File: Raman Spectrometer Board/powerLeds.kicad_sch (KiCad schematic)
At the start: 6 parts

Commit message: tof voltages connected
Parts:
- D1, D2, D3: footprint LED_SMD:LED_0201_0603Metric_Pad0.64x0.40mm_HandSolder -> (none)
- R1, R2, R3: footprint Resistor_SMD:R_0201_0603Metric_Pad0.64x0.40mm_HandSolder -> (none)
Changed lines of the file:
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@@
 			)
 		)
-		(property "Footprint" "LED_SMD:LED_0201_0603Metric_Pad0.64x0.40mm_HandSolder"
+		(property "Footprint" ""
 			(at 123.19 93.98 0)
 			(effects
@@
 			)
 		)
-		(property "Footprint" "LED_SMD:LED_0201_0603Metric_Pad0.64x0.40mm_HandSolder"
+		(property "Footprint" ""
 			(at 138.43 93.98 0)
 			(effects
@@
 			)
 		)
-		(property "Footprint" "Resistor_SMD:R_0201_0603Metric_Pad0.64x0.40mm_HandSolder"
+		(property "Footprint" ""
 			(at 155.956 108.204 90)
 			(effects
@@
 			)
 		)
-		(property "Footprint" "LED_SMD:LED_0201_0603Metric_Pad0.64x0.40mm_HandSolder"
+		(property "Footprint" ""
 			(at 154.94 93.98 0)
 			(effects
@@
 			)
 		)
-		(property "Footprint" "Resistor_SMD:R_0201_0603Metric_Pad0.64x0.40mm_HandSolder"
+		(property "Footprint" ""
 			(at 139.446 108.204 90)
 			(effects
@@
 			)
 		)
-		(property "Footprint" "Resistor_SMD:R_0201_0603Metric_Pad0.64x0.40mm_HandSolder"
+		(property "Footprint" ""
 			(at 124.206 108.204 90)
 			(effects

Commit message: Added footprints to main board
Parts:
- D1, D2, D3: footprint (none) -> LED_SMD:LED_0201_0603Metric_Pad0.64x0.40mm_HandSolder
- R1, R2, R3: footprint (none) -> Resistor_SMD:R_0201_0603Metric_Pad0.64x0.40mm_HandSolder
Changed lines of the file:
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@@
 			)
 		)
-		(property "Footprint" ""
+		(property "Footprint" "LED_SMD:LED_0201_0603Metric_Pad0.64x0.40mm_HandSolder"
 			(at 123.19 93.98 0)
 			(effects
@@
 			)
 		)
-		(property "Footprint" ""
+		(property "Footprint" "LED_SMD:LED_0201_0603Metric_Pad0.64x0.40mm_HandSolder"
 			(at 138.43 93.98 0)
 			(effects
@@
 			)
 		)
-		(property "Footprint" ""
+		(property "Footprint" "Resistor_SMD:R_0201_0603Metric_Pad0.64x0.40mm_HandSolder"
 			(at 155.956 108.204 90)
 			(effects
@@
 			)
 		)
-		(property "Footprint" ""
+		(property "Footprint" "LED_SMD:LED_0201_0603Metric_Pad0.64x0.40mm_HandSolder"
 			(at 154.94 93.98 0)
 			(effects
@@
 			)
 		)
-		(property "Footprint" ""
+		(property "Footprint" "Resistor_SMD:R_0201_0603Metric_Pad0.64x0.40mm_HandSolder"
 			(at 139.446 108.204 90)
 			(effects
@@
 			)
 		)
-		(property "Footprint" ""
+		(property "Footprint" "Resistor_SMD:R_0201_0603Metric_Pad0.64x0.40mm_HandSolder"
 			(at 124.206 108.204 90)
 			(effects

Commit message: Page Consolidation
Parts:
- added C6, C7: 10uF, Capacitor_SMD:C_0603_1608Metric_Pad1.08x0.95mm_HandSolder, symbol Device:C
- added Conn11, Conn4, Conn6: AndersonPP, MRDT_Connectors:Anderson_2_Horizontal_Side_by_Side_PV, symbol MRDT_Connectors:AndersonPP
- added U4: OKI, MRDT_Devices:OKI_Horizontal, symbol MRDT_Devices:OKI
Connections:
- net +12V: now also C6.1, Conn11.4 (PV+), Conn4.4 (PV+), Conn6.4 (PV+), U4.1 (Vi)
- net +5V: now also C7.1, U4.3 (Vo)
- net GND: now also C6.2, C7.2, Conn11.1 (GND), Conn4.1 (GND), Conn6.1 (GND), U4.2 (GND)
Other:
- moved on the sheet: D1, D2, D3, R1, R2, R3

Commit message: Fix Layout Issues
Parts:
- Conn11, Conn4, Conn6: footprint MRDT_Connectors:Anderson_2_Horizontal_Side_by_Side_PV -> MRDT_Connectors:Square_Anderson_2_H_Side_By_Side_PV
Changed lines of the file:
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@@
 			)
 		)
-		(property "Footprint" "MRDT_Connectors:Anderson_2_Horizontal_Side_by_Side_PV"
+		(property "Footprint" "MRDT_Connectors:Square_Anderson_2_H_Side_By_Side_PV"
 			(at 133.35 87.63 0)
 			(effects
@@
 			)
 		)
-		(property "Footprint" "MRDT_Connectors:Anderson_2_Horizontal_Side_by_Side_PV"
+		(property "Footprint" "MRDT_Connectors:Square_Anderson_2_H_Side_By_Side_PV"
 			(at 36.83 87.63 0)
 			(effects
@@
 			)
 		)
-		(property "Footprint" "MRDT_Connectors:Anderson_2_Horizontal_Side_by_Side_PV"
+		(property "Footprint" "MRDT_Connectors:Square_Anderson_2_H_Side_By_Side_PV"
 			(at 133.35 72.39 0)
 			(effects
@@
 			)
 		)
-		(property "Footprint" "MRDT_Connectors:Anderson_2_Horizontal_Side_by_Side_PV"
+		(property "Footprint" "MRDT_Connectors:Square_Anderson_2_H_Side_By_Side_PV"
 			(at 71.12 72.39 0)
 			(effects
@@
 			)
 		)
-		(property "Footprint" "MRDT_Connectors:Anderson_2_Horizontal_Side_by_Side_PV"
+		(property "Footprint" "MRDT_Connectors:Square_Anderson_2_H_Side_By_Side_PV"
 			(at 71.12 87.63 0)
 			(effects
@@
 			)
 		)
-		(property "Footprint" "MRDT_Connectors:Anderson_2_Horizontal_Side_by_Side_PV"
+		(property "Footprint" "MRDT_Connectors:Square_Anderson_2_H_Side_By_Side_PV"
 			(at 36.83 72.39 0)
 			(effects

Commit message: Initial layout
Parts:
- added Q6: AO3401A, Package_TO_SOT_SMD:SOT-23, symbol Transistor_FET:AO3401A
- added R19: 10k, symbol Device:R_US
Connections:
- net +12V: now also Q6.2 (S); no longer Conn11.4 (PV+)
- net GND: now also R19.2
- new net: Q6.1 (G), R19.1
- new net: Conn11.4 (PV+), Q6.3 (D)
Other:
- moved on the sheet: Conn11D
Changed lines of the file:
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@@
+	)
+	(junction
+		(at 168.91 71.12)
+		(diameter 0)
+		(color 0 0 0 0)
 	)
 	(junction
@@
 	(wire
 		(pts
+			(xy 168.91 60.96) (xy 168.91 62.23)
+		)
+		(stroke
+			(width 0)
+			(type default)
+		)
+	)
+	(wire
+		(pts
 			(xy 139.7 154.94) (xy 139.7 162.56)
 		)
@@
 	(wire
 		(pts
+			(xy 168.91 69.85) (xy 168.91 71.12)
+		)
+		(stroke
+			(width 0)
+			(type default)
+		)
+	)
+	(wire
+		(pts
 			(xy 123.19 161.29) (xy 123.19 162.56)
 		)
@@
 	(wire
 		(pts
-			(xy 152.4 55.88) (xy 147.32 55.88)
+			(xy 173.99 53.34) (xy 190.5 53.34)
 		)
 		(stroke
@@
 	(wire
 		(pts
+			(xy 190.5 53.34) (xy 190.5 46.99)
+		)
+		(stroke
+			(width 0)
+			(type default)
+		)
+	)
+	(wire
+		(pts
 			(xy 90.17 48.26) (xy 90.17 55.88)
 		)
@@
 	(wire
 		(pts
-			(xy 152.4 71.12) (xy 152.4 78.74)
+			(xy 184.15 71.12) (xy 184.15 81.28)
 		)
 		(stroke
@@
 	(wire
 		(pts
+			(xy 184.15 71.12) (xy 168.91 71.12)
+		)
+		(stroke
+			(width 0)
+			(type default)
+		)
+	)
+	(wire
+		(pts
 			(xy 55.88 48.26) (xy 55.88 55.88)
 		)
@@
 	(wire
 		(pts
-			(xy 152.4 48.26) (xy 152.4 55.88)
-		)
-		(stroke
-			(width 0)
-			(type default)
-		)
-	)
-	(wire
-		(pts
 			(xy 50.8 71.12) (xy 55.88 71.12)
 		)
@@
 	(wire
 		(pts
-			(xy 147.32 71.12) (xy 152.4 71.12)
+			(xy 147.32 71.12) (xy 168.91 71.12)
+		)
+		(stroke
+			(width 0)
+			(type default)
+		)
+	)
+	(wire
+		(pts
+			(xy 147.32 53.34) (xy 163.83 53.34)
 		)
 		(stroke
@@
 	)
 	(symbol
+		(lib_id "Transistor_FET:AO3401A")
+		(at 168.91 55.88 90)
+		(unit 1)
+		(exclude_from_sim no)
+		(in_bom yes)
+		(on_board yes)
+		(dnp no)
+		(fields_autoplaced yes)
+		(property "Reference" "Q6"
+			(at 168.91 46.99 90)
+			(effects
+				(font
+					(size 1.27 1.27)
+				)
+			)
+		)
+		(property "Value" "AO3401A"
+			(at 168.91 49.53 90)
+			(effects
+				(font
+					(size 1.27 1.27)
+				)
+			)
+		)
+		(property "Footprint" "Package_TO_SOT_SMD:SOT-23"
+			(at 170.815 50.8 0)
+			(effects
+				(font
+					(size 1.27 1.27)
+					(italic yes)
+				)
+				(justify left)
+				(hide yes)
+			)
+		)
+		(property "Datasheet" "http://www.aosmd.com/pdfs/datasheet/AO3401A.pdf"
+			(at 172.72 50.8 0)
+			(effects
+				(font
+					(size 1.27 1.27)
+				)
+				(justify left)
+				(hide yes)
+			)
+		)
+		(property "Description" "-4.0A Id, -30V Vds, P-Channel MOSFET, SOT-23"
+			(at 168.91 55.88 0)
+			(effects
+				(font
+					(size 1.27 1.27)
+				)
+				(hide yes)
+			)
+		)
+		(pin "3"
+		)
+		(pin "2"
+		)
+		(pin "1"
+		)
+		(instances
+			(project "RamanSpectrometerBoard"
+				(path "/ab487c59-f066-48f5-a383-99e8eaf806bf/53169187-8b1b-4ef9-9158-1480f8ad4334"
+					(reference "Q6")
+					(unit 1)
+				)
+			)
+		)
+	)
+	(symbol
 		(lib_id "power:GND")
 		(at 90.17 78.74 0)
@@
 	(symbol
 		(lib_id "MRDT_Connectors:AndersonPP")
-		(at 137.16 58.42 0)
+		(at 137.16 55.88 0)
 		(unit 4)
 		(exclude_from_sim no)
@@
 		(fields_autoplaced yes)
 		(property "Reference" "Conn11"
+			(at 139.7 45.72 0)
+			(effects
+				(font
+					(size 1.524 1.524)
+				)
+			)
+		)
+		(property "Value" "AndersonPP"
 			(at 139.7 48.26 0)
 			(effects
@@
 			)
 		)
-		(property "Value" "AndersonPP"
-			(at 139.7 50.8 0)
-			(effects
-				(font
-					(size 1.524 1.524)
-				)
-			)
-		)
 		(property "Footprint" "MRDT_Connectors:Square_Anderson_2_H_Side_By_Side_PV"
-			(at 133.35 72.39 0)
+			(at 133.35 69.85 0)
 			(effects
 				(font
@@
 		)
 		(property "Datasheet" ""
-			(at 133.35 72.39 0)
+			(at 133.35 69.85 0)
 			(effects
 				(font
@@
 		)
 		(property "Description" ""
-			(at 137.16 58.42 0)
+			(at 137.16 55.88 0)
 			(effects
 				(font
@@
 	(symbol
 		(lib_id "power:+12V")
-		(at 152.4 48.26 0)
+		(at 190.5 46.99 0)
 		(unit 1)
 		(exclude_from_sim no)
@@
 		(fields_autoplaced yes)
 		(property "Reference" "#PWR044"
-			(at 152.4 52.07 0)
+			(at 190.5 50.8 0)
 			(effects
 				(font
@@
 		)
 		(property "Value" "+12V"
-			(at 152.4 43.18 0)
+			(at 190.5 41.91 0)
 			(effects
 				(font
@@
 		)
 		(property "Footprint" ""
-			(at 152.4 48.26 0)
+			(at 190.5 46.99 0)
 			(effects
 				(font
@@
 		)
 		(property "Datasheet" ""
-			(at 152.4 48.26 0)
+			(at 190.5 46.99 0)
 			(effects
 				(font
@@
 		)
 		(property "Description" "Power symbol creates a global label with name \"+12V\""
-			(at 152.4 48.26 0)
+			(at 190.5 46.99 0)
 			(effects
 				(font
@@
 	(symbol
 		(lib_id "power:GND")
-		(at 152.4 78.74 0)
+		(at 184.15 81.28 0)
 		(unit 1)
 		(exclude_from_sim no)
@@
 		(fields_autoplaced yes)
 		(property "Reference" "#PWR045"
-			(at 152.4 85.09 0)
+			(at 184.15 87.63 0)
 			(effects
 				(font
@@
 		)
 		(property "Value" "GND"
-			(at 152.4 83.82 0)
+			(at 184.15 86.36 0)
 			(effects
 				(font
@@
 		)
 		(property "Footprint" ""
-			(at 152.4 78.74 0)
+			(at 184.15 81.28 0)
 			(effects
 				(font
@@
 		)
 		(property "Datasheet" ""
-			(at 152.4 78.74 0)
+			(at 184.15 81.28 0)
 			(effects
 				(font
@@
 		)
 		(property "Description" "Power symbol creates a global label with name \"GND\" , ground"
-			(at 152.4 78.74 0)
+			(at 184.15 81.28 0)
 			(effects
 				(font
@@
 					(unit 1)
 				)
+			)
+		)
+	)
+	(symbol
+		(lib_id "Device:R_US")
+		(at 168.91 66.04 0)
+		(unit 1)
+		(exclude_from_sim no)
+		(in_bom yes)
+		(on_board yes)
+		(dnp no)
+		(fields_autoplaced yes)
+		(property "Reference" "R19"
+			(at 171.45 64.7699 0)
+			(effects
+				(font
+					(size 1.27 1.27)
+				)
+				(justify left)
+			)
+		)
+		(property "Value" "10k"
+			(at 171.45 67.3099 0)
+			(effects
+				(font
+					(size 1.27 1.27)
+				)
+				(justify left)
+			)
+		)
+		(property "Footprint" ""
+			(at 169.926 66.294 90)
+			(effects
+				(font
+					(size 1.27 1.27)
+				)
+				(hide yes)
+			)
+		)
+		(property "Datasheet" "~"
+			(at 168.91 66.04 0)
+			(effects
+				(font
+					(size 1.27 1.27)
+				)
+				(hide yes)
+			)
+		)
+		(property "Description" "Resistor, US symbol"
+			(at 168.91 66.04 0)
+			(effects
+				(font
+					(size 1.27 1.27)
+				)
+				(hide yes)
+			)
+		)
+		(pin "2"
+		)
+		(pin "1"
+		)
+		(instances
+			(project ""
+				(path "/ab487c59-f066-48f5-a383-99e8eaf806bf/53169187-8b1b-4ef9-9158-1480f8ad4334"
+					(reference "R19")
+					(unit 1)
+				)

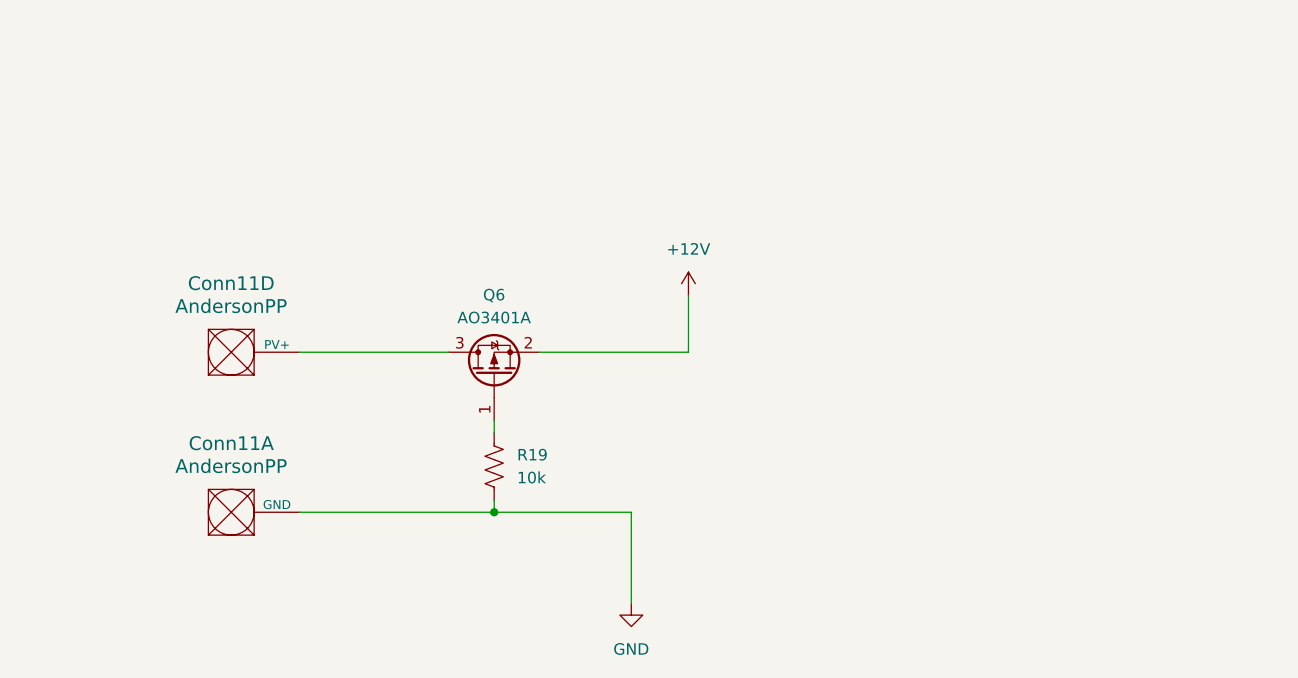
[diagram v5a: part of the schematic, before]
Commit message: Added Reverse Voltage Protection
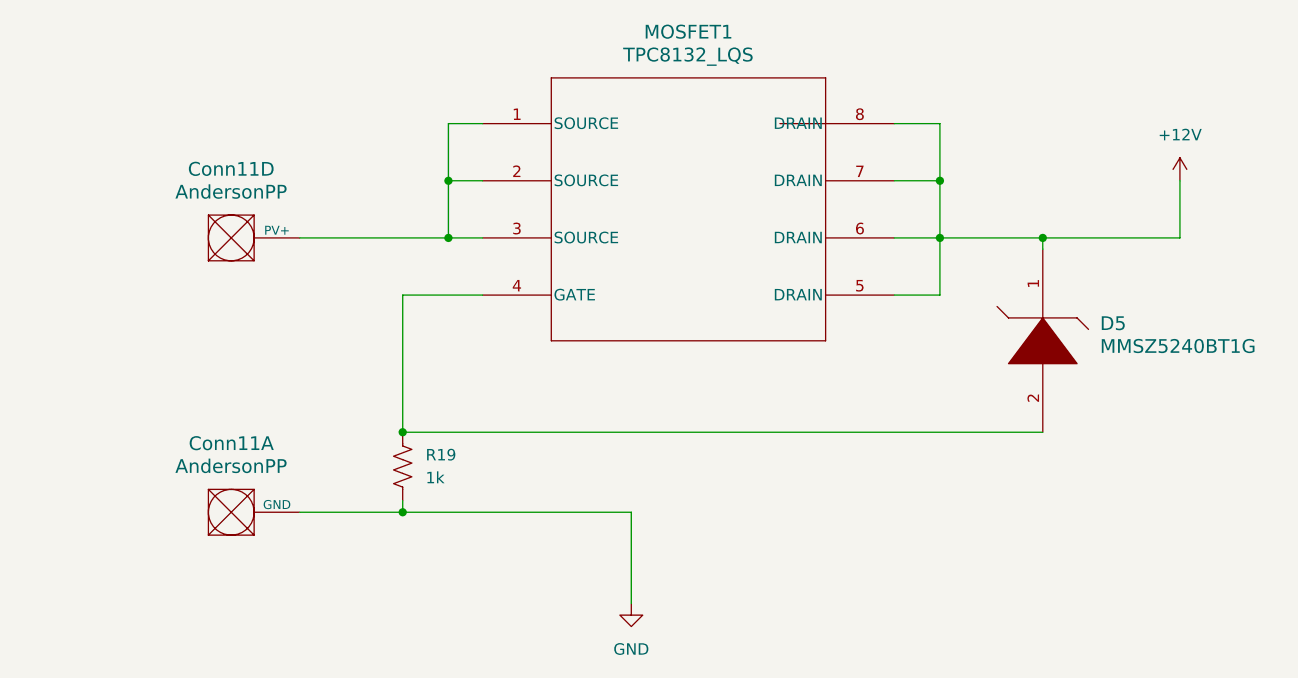
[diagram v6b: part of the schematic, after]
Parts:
- removed Q6: AO3401A, Package_TO_SOT_SMD:SOT-23, symbol Transistor_FET:AO3401A
- added D5: MMSZ5240BT1G, MRDT_Devices:SOD-123_ONS-L, symbol MRDT_Devices:MMSZ5240BT1G
- added MOSFET1: TPC8132_LQS, MRDT_Devices:SOP-8_TOS-L, symbol MRDT_Devices:TPC8132_LQS
- R19: value 10k -> 1k; footprint (none) -> Resistor_SMD:R_0603_1608Metric_Pad0.98x0.95mm_HandSolder
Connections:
- net +12V: now also D5.1, MOSFET1.5 (DRAIN), MOSFET1.6 (DRAIN), MOSFET1.7 (DRAIN), MOSFET1.8 (DRAIN)
- net at R19.1: now also D5.2, MOSFET1.4 (GATE)
- net at Conn11.4 (PV+): now also MOSFET1.1 (SOURCE), MOSFET1.2 (SOURCE), MOSFET1.3 (SOURCE)
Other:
- moved on the sheet: Conn11D, R19
